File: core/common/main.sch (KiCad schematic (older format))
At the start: 6 parts, among them P1 CONN_01X05, P2 CONN_01X03, P3 CONN_01X02, P4 CONN_01X02, U1 NDSL_DPad, U2 NDSL_SS

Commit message: updated for ndsl_dpad, ndsl_ss, ndsl_lr, n900_keyboard
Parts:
- added U3: N900_Keyboard, steward:MyFT_N900_Keyboard, symbol N900_Keyboard
- P3: footprint steward:MyFT_Pad_Circle -> Buttons_Switches_SMD:SW_SPST_EVPBF
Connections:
- net DC: now also U1.5
- net DL: now also U1.3
- net DR: now also U1.4
- net DU: now also U1.1
- net DW: now also U1.2
- net SC: now also U2.2, U2.4
- net SS: now also U2.1
- net ST: now also U2.3
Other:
- moved on the sheet: P1, P2, P3, P4, U1, U2
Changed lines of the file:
@@
 L NDSL_DPad U1
 U 1 1 5B729574
-P 3050 3350
-F 0 "U1" H 2800 3750 60  0000 C CNN
-F 1 "NDSL_DPad" H 3000 3650 60  0000 C CNN
-F 2 "steward:MyFT_NDSL_DPad" H 3200 3550 60  0001 C CNN
-F 3 "" H 3200 3550 60  0000 C CNN
-	1    3050 3350
+P 3050 3250
+F 0 "U1" H 2800 3650 60  0000 C CNN
+F 1 "NDSL_DPad" H 3000 3550 60  0000 C CNN
+F 2 "steward:MyFT_NDSL_DPad" H 3200 3450 60  0001 C CNN
+F 3 "" H 3200 3450 60  0000 C CNN
+	1    3050 3250
 	1    0    0    -1
 $EndComp
@@
 L CONN_01X05 P1
 U 1 1 5B7295AF
-P 3100 4250
-F 0 "P1" H 3100 4550 50  0000 C CNN
-F 1 "CONN_01X05" V 3200 4250 50  0000 C CNN
-F 2 "steward:MyFT_SIM5" H 3100 4250 50  0001 C CNN
-F 3 "" H 3100 4250 50  0000 C CNN
-	1    3100 4250
+P 3100 4150
+F 0 "P1" H 3100 4450 50  0000 C CNN
+F 1 "CONN_01X05" V 3200 4150 50  0000 C CNN
+F 2 "steward:MyFT_SIM5" H 3100 4150 50  0001 C CNN
+F 3 "" H 3100 4150 50  0000 C CNN
+	1    3100 4150
 	0    -1   -1   0
 $EndComp
@@
 L NDSL_SS U2
 U 1 1 5B7295E0
-P 4000 3350
-F 0 "U2" H 3800 3750 60  0000 C CNN
-F 1 "NDSL_SS" H 3950 3650 60  0000 C CNN
-F 2 "steward:MyFT_NDSL_SS" H 4200 3550 60  0001 C CNN
-F 3 "" H 4200 3550 60  0000 C CNN
-	1    4000 3350
+P 4500 3600
+F 0 "U2" H 4300 4000 60  0000 C CNN
+F 1 "NDSL_SS" H 4450 3900 60  0000 C CNN
+F 2 "steward:MyFT_NDSL_SS" H 4700 3800 60  0001 C CNN
+F 3 "" H 4700 3800 60  0000 C CNN
+	1    4500 3600
 	1    0    0    -1
 $EndComp
@@
 L CONN_01X03 P2
 U 1 1 5B729609
-P 4000 4250
-F 0 "P2" H 4000 4450 50  0000 C CNN
-F 1 "CONN_01X03" V 4100 4250 50  0000 C CNN
-F 2 "steward:MyFT_SIM3" H 4000 4250 50  0001 C CNN
-F 3 "" H 4000 4250 50  0000 C CNN
-	1    4000 4250
+P 4500 3950
+F 0 "P2" H 4500 4150 50  0000 C CNN
+F 1 "CONN_01X03" V 4600 3950 50  0000 C CNN
+F 2 "steward:MyFT_SIM3" H 4500 3950 50  0001 C CNN
+F 3 "" H 4500 3950 50  0000 C CNN
+	1    4500 3950
 	0    -1   -1   0
 $EndComp
@@
 L CONN_01X02 P3
 U 1 1 5B729640
-P 4800 3450
-F 0 "P3" H 4800 3600 50  0000 C CNN
-F 1 "CONN_01X02" V 4900 3450 50  0000 C CNN
-F 2 "steward:MyFT_Pad_Circle" H 4800 3450 50  0001 C CNN
-F 3 "" H 4800 3450 50  0000 C CNN
-	1    4800 3450
+P 5700 3250
+F 0 "P3" H 5700 3400 50  0000 C CNN
+F 1 "CONN_01X02" V 5800 3250 50  0000 C CNN
+F 2 "Buttons_Switches_SMD:SW_SPST_EVPBF" H 5700 3250 50  0001 C CNN
+F 3 "" H 5700 3250 50  0000 C CNN
+	1    5700 3250
 	0    -1   -1   0
 $EndComp
@@
 L CONN_01X02 P4
 U 1 1 5B72967B
-P 4800 4250
-F 0 "P4" H 4800 4400 50  0000 C CNN
-F 1 "CONN_01X02" V 4900 4250 50  0000 C CNN
-F 2 "steward:MyFT_SIM2" H 4800 4250 50  0001 C CNN
-F 3 "" H 4800 4250 50  0000 C CNN
-	1    4800 4250
+P 5700 4050
+F 0 "P4" H 5700 4200 50  0000 C CNN
+F 1 "CONN_01X02" V 5800 4050 50  0000 C CNN
+F 2 "steward:MyFT_SIM2" H 5700 4050 50  0001 C CNN
+F 3 "" H 5700 4050 50  0000 C CNN
+	1    5700 4050
 	0    -1   -1   0
 $EndComp
-Text GLabel 2850 3750 3    60   Input ~ 0
+Text GLabel 3050 2900 1    60   Input ~ 0
 DU
-Text GLabel 2950 3750 3    60   Input ~ 0
+Text GLabel 3050 3600 3    60   Input ~ 0
 DW
-Text GLabel 3050 3750 3    60   Input ~ 0
+Text GLabel 2700 3250 0    60   Input ~ 0
 DL
-Text GLabel 3150 3750 3    60   Input ~ 0
+Text GLabel 3400 3250 2    60   Input ~ 0
 DR
-Text GLabel 3300 3750 3    60   Input ~ 0
+Text GLabel 3200 3600 3    60   Input ~ 0
 DC
-Text GLabel 3850 3750 3    60   Input ~ 0
+Text GLabel 4200 3450 0    60   Input ~ 0
 SS
-Text GLabel 4050 3750 3    60   Input ~ 0
+Text GLabel 4800 3450 2    60   Input ~ 0
 ST
-Text GLabel 3950 3750 3    60   Input ~ 0
+Text GLabel 4200 3600 0    60   Input ~ 0
 SC
-Text GLabel 3000 4450 3    60   Input ~ 0
+Text GLabel 3000 4350 3    60   Input ~ 0
 DU
-Text GLabel 3100 4450 3    60   Input ~ 0
+Text GLabel 3100 4350 3    60   Input ~ 0
 DW
-Text GLabel 2900 4450 3    60   Input ~ 0
+Text GLabel 2900 4350 3    60   Input ~ 0
 DL
-Text GLabel 3200 4450 3    60   Input ~ 0
+Text GLabel 3200 4350 3    60   Input ~ 0
 DR
-Text GLabel 3300 4450 3    60   Input ~ 0
+Text GLabel 3300 4350 3    60   Input ~ 0
 DC
-Text GLabel 4100 4450 3    60   Input ~ 0
+Text GLabel 4600 4150 3    60   Input ~ 0
 SS
-Text GLabel 3900 4450 3    60   Input ~ 0
+Text GLabel 4400 4150 3    60   Input ~ 0
 ST
-Text GLabel 4000 4450 3    60   Input ~ 0
+Text GLabel 4500 4150 3    60   Input ~ 0
 SC
-Text GLabel 4750 3650 3    60   Input ~ 0
+Text GLabel 5650 3450 3    60   Input ~ 0
 B1
-Text GLabel 4850 3650 3    60   Input ~ 0
+Text GLabel 5750 3450 3    60   Input ~ 0
 B2
-Text GLabel 4750 4450 3    60   Input ~ 0
+Text GLabel 5650 4250 3    60   Input ~ 0
 B1
-Text GLabel 4850 4450 3    60   Input ~ 0
+Text GLabel 5750 4250 3    60   Input ~ 0
 B2
-Text GLabel 4150 3750 3    60   Input ~ 0
+Text GLabel 4800 3600 2    60   Input ~ 0
 SC
+$Comp
+L N900_Keyboard U3
+U 1 1 5BC05391
+P 7400 3900
+F 0 "U3" H 6625 4650 60  0000 C CNN
+F 1 "N900_Keyboard" H 6925 4575 60  0000 C CNN
+F 2 "steward:MyFT_N900_Keyboard" H 7600 4000 60  0000 C CNN
+F 3 "" H 7600 4000 60  0000 C CNN
+	1    7400 3900
+	1    0    0    -1
+$EndComp
 $EndSCHEMATC

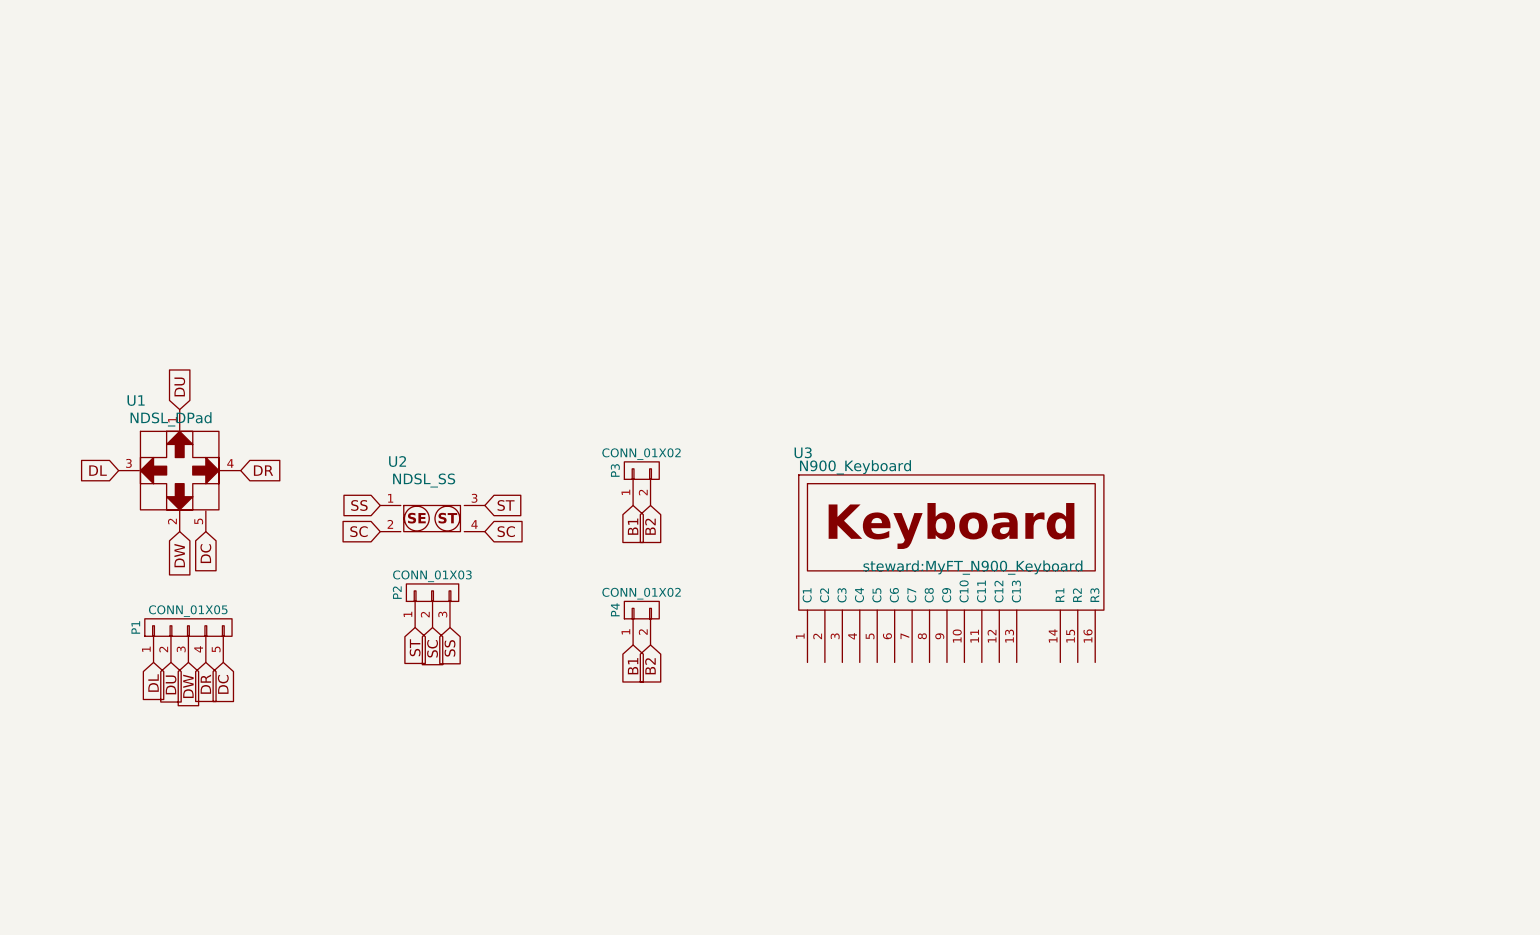
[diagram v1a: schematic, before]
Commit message: updated n900 and blackberry q30 sch & pcb
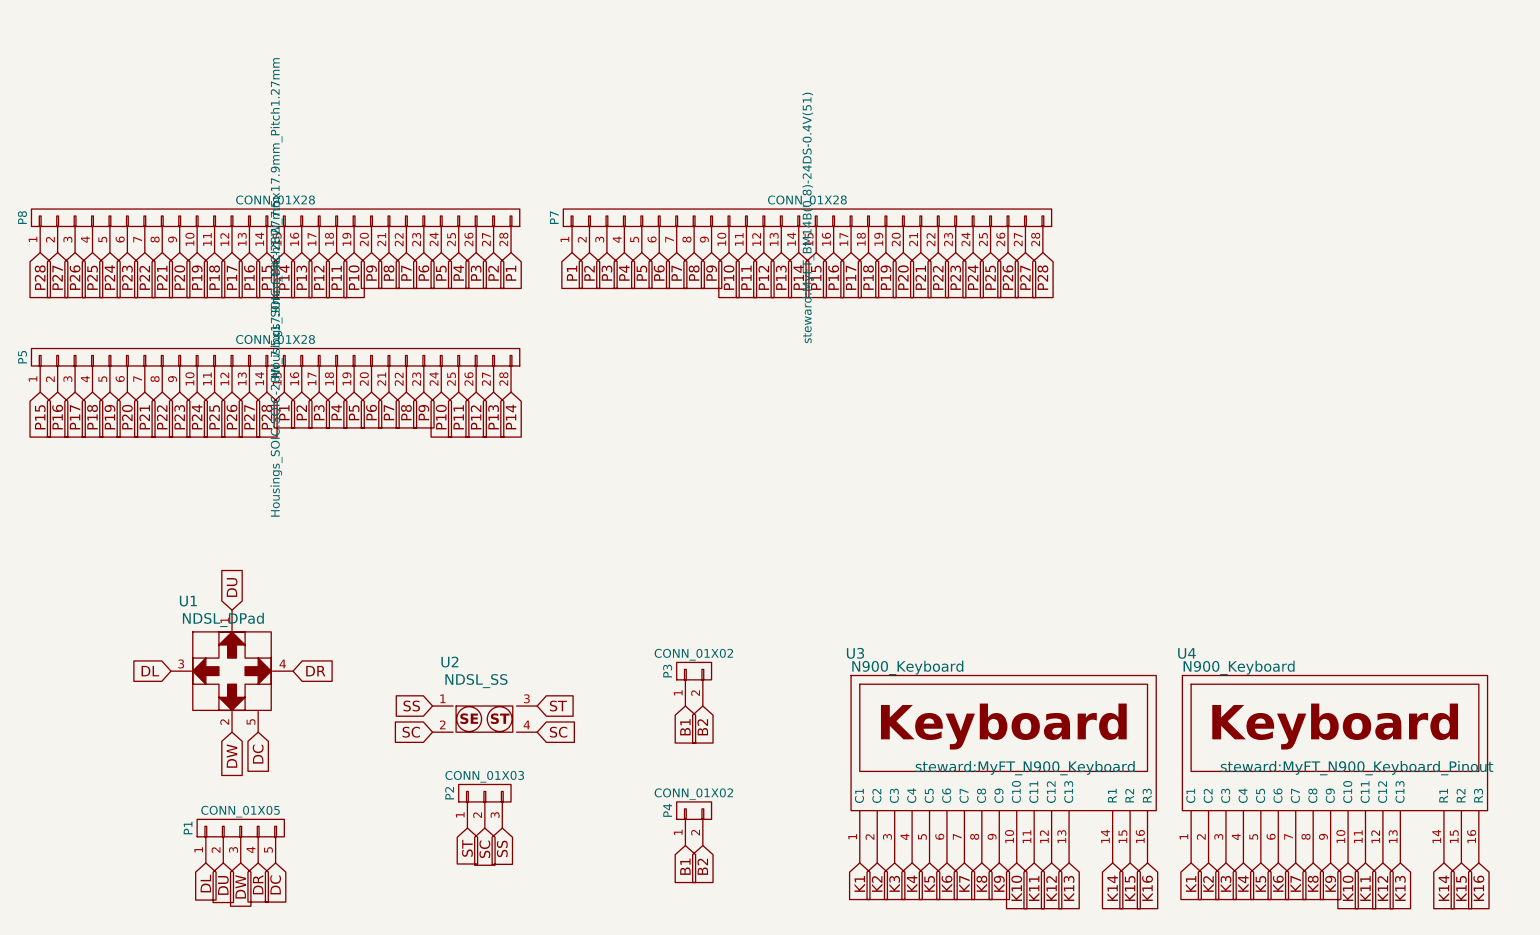
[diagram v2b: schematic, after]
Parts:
- added P5, P8: CONN_01X28, Housings_SOIC:SOIC-28W_7.5x17.9mm_Pitch1.27mm, symbol CONN_01X28
- added P7: CONN_01X28, steward:MyFT_BM14B(0.8)-24DS-0.4V(51), symbol CONN_01X28
- added U4: N900_Keyboard, steward:MyFT_N900_Keyboard_Pinout, symbol N900_Keyboard
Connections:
- net K1: now reaches U3.1 (C1)
- net K1: now also U4.1 (C1)
- net K10: now reaches U3.10 (C10)
- net K10: now also U4.10 (C10)
- net K11: now reaches U3.11 (C11)
- net K11: now also U4.11 (C11)
- net K12: now reaches U3.12 (C12)
- net K12: now also U4.12 (C12)
- net K13: now reaches U3.13 (C13)
- net K13: now also U4.13 (C13)
- net K14: now reaches U3.14 (R1)
- net K14: now also U4.14 (R1)
- net K15: now reaches U3.15 (R2)
- net K15: now also U4.15 (R2)
- net K16: now reaches U3.16 (R3)
- net K16: now also U4.16 (R3)
- net K2: now reaches U3.2 (C2)
- net K2: now also U4.2 (C2)
- net K3: now reaches U3.3 (C3)
- net K3: now also U4.3 (C3)
- net K4: now reaches U3.4 (C4)
- net K4: now also U4.4 (C4)
- net K5: now reaches U3.5 (C5)
- net K5: now also U4.5 (C5)
- net K6: now reaches U3.6 (C6)
- net K6: now also U4.6 (C6)
- net K7: now reaches U3.7 (C7)
- net K7: now also U4.7 (C7)
- net K8: now reaches U3.8 (C8)
- net K8: now also U4.8 (C8)
- net K9: now reaches U3.9 (C9)
- net K9: now also U4.9 (C9)
- new net P1: P5.15 (P15), P7.1 (P1), P8.28 (P28)
- new net P10: P5.24 (P24), P7.10 (P10), P8.19 (P19)
- new net P11: P5.25 (P25), P7.11 (P11), P8.18 (P18)
- new net P12: P5.26 (P26), P7.12 (P12), P8.17 (P17)
- new net P13: P5.27 (P27), P7.13 (P13), P8.16 (P16)
- new net P14: P5.28 (P28), P7.14 (P14), P8.15 (P15)
- new net P15: P5.1 (P1), P7.15 (P15), P8.14 (P14)
- new net P16: P5.2 (P2), P7.16 (P16), P8.13 (P13)
- new net P17: P5.3 (P3), P7.17 (P17), P8.12 (P12)
- new net P18: P5.4 (P4), P7.18 (P18), P8.11 (P11)
- new net P19: P5.5 (P5), P7.19 (P19), P8.10 (P10)
- new net P2: P5.16 (P16), P7.2 (P2), P8.27 (P27)
- new net P20: P5.6 (P6), P7.20 (P20), P8.9 (P9)
- new net P21: P5.7 (P7), P7.21 (P21), P8.8 (P8)
- new net P22: P5.8 (P8), P7.22 (P22), P8.7 (P7)
- new net P23: P5.9 (P9), P7.23 (P23), P8.6 (P6)
- new net P24: P5.10 (P10), P7.24 (P24), P8.5 (P5)
- new net P25: P5.11 (P11), P7.25 (P25), P8.4 (P4)
- new net P26: P5.12 (P12), P7.26 (P26), P8.3 (P3)
- new net P27: P5.13 (P13), P7.27 (P27), P8.2 (P2)
- new net P28: P5.14 (P14), P7.28 (P28), P8.1 (P1)
- new net P3: P5.17 (P17), P7.3 (P3), P8.26 (P26)
- new net P4: P5.18 (P18), P7.4 (P4), P8.25 (P25)
- new net P5: P5.19 (P19), P7.5 (P5), P8.24 (P24)
- new net P6: P5.20 (P20), P7.6 (P6), P8.23 (P23)
- new net P7: P5.21 (P21), P7.7 (P7), P8.22 (P22)
- new net P8: P5.22 (P22), P7.8 (P8), P8.21 (P21)
- new net P9: P5.23 (P23), P7.9 (P9), P8.20 (P20)
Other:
- moved on the sheet: P1, P2, P3, P4, U1, U2, U3

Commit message: updated n900 pcb
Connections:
- net K1: now also U4.13 (C13); no longer U4.1 (C1)
- net K10: now also U4.4 (C4); no longer U4.10 (C10)
- net K11: now also U4.3 (C3); no longer U4.11 (C11)
- net K12: now also U4.2 (C2); no longer U4.12 (C12)
- net K13: now also U4.1 (C1); no longer U4.13 (C13)
- net K2: now also U4.12 (C12); no longer U4.2 (C2)
- net K3: now also U4.11 (C11); no longer U4.3 (C3)
- net K4: now also U4.10 (C10); no longer U4.4 (C4)
- net K5: now also U4.9 (C9); no longer U4.5 (C5)
- net K6: now also U4.8 (C8); no longer U4.6 (C6)
- net K8: now also U4.6 (C6); no longer U4.8 (C8)
- net K9: now also U4.5 (C5); no longer U4.9 (C9)
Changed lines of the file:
@@
 Text GLabel 8600 5500 3    60   Input ~ 0
 K16
-Text GLabel 8850 5500 3    60   Input ~ 0
+Text GLabel 10050 5500 3    60   Input ~ 0
 K1
-Text GLabel 8950 5500 3    60   Input ~ 0
+Text GLabel 9950 5500 3    60   Input ~ 0
 K2
-Text GLabel 9050 5500 3    60   Input ~ 0
+Text GLabel 9850 5500 3    60   Input ~ 0
 K3
-Text GLabel 9150 5500 3    60   Input ~ 0
+Text GLabel 9750 5500 3    60   Input ~ 0
 K4
-Text GLabel 9250 5500 3    60   Input ~ 0
+Text GLabel 9650 5500 3    60   Input ~ 0
 K5
-Text GLabel 9350 5500 3    60   Input ~ 0
+Text GLabel 9550 5500 3    60   Input ~ 0
 K6
 Text GLabel 9450 5500 3    60   Input ~ 0
 K7
-Text GLabel 9550 5500 3    60   Input ~ 0
+Text GLabel 9350 5500 3    60   Input ~ 0
 K8
-Text GLabel 9650 5500 3    60   Input ~ 0
+Text GLabel 9250 5500 3    60   Input ~ 0
 K9
-Text GLabel 9750 5500 3    60   Input ~ 0
+Text GLabel 9150 5500 3    60   Input ~ 0
 K10
-Text GLabel 9850 5500 3    60   Input ~ 0
+Text GLabel 9050 5500 3    60   Input ~ 0
 K11
-Text GLabel 9950 5500 3    60   Input ~ 0
+Text GLabel 8950 5500 3    60   Input ~ 0
 K12
-Text GLabel 10050 5500 3    60   Input ~ 0
+Text GLabel 8850 5500 3    60   Input ~ 0
 K13
 Text GLabel 10300 5500 3    60   Input ~ 0
